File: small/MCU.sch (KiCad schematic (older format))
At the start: 35 parts, among them IC1 PIC32MX350F256H-V_PT, J3 Micro_SD_Card, J4 Conn_01x05_Female, U5 AT25M02, U8 PCF8563T, Y2 Crystal

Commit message: BOM updated
Layout changed
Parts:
- C15, C17, C18, C19, C20, C21, C24, C29, C30, C31: source (none) -> 0
- C25: source (none) -> 1
- C26, C44: value 15pf -> 20pf; MPN (none) -> CL10C200JB8NNNC; source (none) -> 0
- D10, D4: MPN (none) -> FC-2012HRK-620D; Price (none) -> 0.0199; source (none) -> 0
- D8: MPN (none) -> SS14; source (none) -> 0
- IC1: MPN (none) -> PIC32MX350F256H-V/PT; Manufacturer_Name Microchip -> (none); Manufacturer_Part_Number PIC32MX350F256H-V/PT -> (none)
- R24: MPN (none) -> 0603WAF1005T5E; Price (none) -> 0.0028; source (none) -> 0
- R39, R7: MPN (none) -> 0603WAF1000T5E; source (none) -> 0
- R5: MPN (none) -> 0603WAF1002T5E; source (none) -> 0
- R6: MPN (none) -> 0603WAF1001T5E; source (none) -> 0
- U5: Website (none) -> mouser; source (none) -> 0
- U8: MPN (none) -> PCF8563T; source (none) -> 0
- Y2: MPN (none) -> Q13FC1350000400; Price (none) -> 0.4291; source (none) -> 0
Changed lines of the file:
@@
 F 4 "C25804" H 1800 3350 50  0001 C CNN "LCSC"
 F 5 "0.02" H 1800 3350 50  0001 C CNN "Price"
+F 6 "0603WAF1002T5E" H 1800 3350 50  0001 C CNN "MPN"
+F 7 "0" H 1800 3350 50  0001 C CNN "source"
 	1    1800 3350
 	0    1    1    0
@@
 F 5 "0.0071" H 1075 3675 50  0001 C CNN "Price"
 F 6 "CC0603KRX7R9BB104" H 1075 3675 50  0001 C CNN "MPN"
+F 7 "0" H 1075 3675 50  0001 C CNN "source"
 	1    1075 3675
 	1    0    0    -1
@@
 F 4 " C21190" H 1800 3450 50  0001 C CNN "LCSC"
 F 5 "0.009" H 1800 3450 50  0001 C CNN "Price"
+F 6 "0603WAF1001T5E" H 1800 3450 50  0001 C CNN "MPN"
+F 7 "0" H 1800 3450 50  0001 C CNN "source"
 	1    1800 3450
 	0    1    1    0
@@
 F 3 "https://datasheet.lcsc.com/szlcsc/Foshan-NationStar-Optoelectronics-FC-2012HRK-620D_C84256.pdf" H 8125 3925 50  0001 C CNN
 F 4 "C84256" V 8125 3925 50  0001 C CNN "LCSC"
+F 5 "FC-2012HRK-620D" H 8125 3925 50  0001 C CNN "MPN"
+F 6 "0.0199" H 8125 3925 50  0001 C CNN "Price"
+F 7 "0" H 8125 3925 50  0001 C CNN "source"
 	1    8125 3925
 	0    -1   -1   0
@@
 F 4 "C22775" H 8125 4225 50  0001 C CNN "LCSC"
 F 5 "0.0019" H 8125 4225 50  0001 C CNN "Price"
+F 6 "0603WAF1000T5E" H 8125 4225 50  0001 C CNN "MPN"
+F 7 "0" H 8125 4225 50  0001 C CNN "source"
 	1    8125 4225
 	1    0    0    -1
@@
 F 4 "C7440" H 9975 5450 50  0001 C CNN "LCSC"
 F 5 "0.3876" H 9975 5450 50  0001 C CNN "Price"
+F 6 "PCF8563T" H 9975 5450 50  0001 C CNN "MPN"
+F 7 "0" H 9975 5450 50  0001 C CNN "source"
 	1    9975 5450
 	1    0    0    -1
@@
 AR Path="/6078415F/607D7927" Ref="C26"  Part="1"
 F 0 "C26" H 9315 5146 50  0000 L CNN
-F 1 "15pf" H 9315 5055 50  0000 L CNN
+F 1 "20pf" H 9315 5055 50  0000 L CNN
 F 2 "Capacitor_SMD:C_0603_1608Metric_Pad1.08x0.95mm_HandSolder" H 9238 4950 50  0001 C CNN
 F 3 "https://datasheet.lcsc.com/szlcsc/Samsung-Electro-Mechanics-CL10C150JB8NNNC_C1644.pdf" H 9200 5100 50  0001 C CNN
 F 4 "C1648" H 9200 5100 50  0001 C CNN "LCSC"
 F 5 "C1644" H 9200 5100 50  0001 C CNN "Price"
+F 6 "CL10C200JB8NNNC" H 9200 5100 50  0001 C CNN "MPN"
+F 7 "0" H 9200 5100 50  0001 C CNN "source"
 	1    9200 5100
 	1    0    0    -1
@@
 F 3 "https://datasheet.lcsc.com/szlcsc/1901081604_Seiko-Epson-Q13FC1350000400_C32346.pdf" H 9200 5450 50  0001 C CNN
 F 4 "C32346" V 9200 5450 50  0001 C CNN "LCSC"
+F 5 "Q13FC1350000400" H 9200 5450 50  0001 C CNN "MPN"
+F 6 "0.4291" H 9200 5450 50  0001 C CNN "Price"
+F 7 "0" H 9200 5450 50  0001 C CNN "source"
 	1    9200 5450
 	0    1    1    0
@@
 F 4 " C2480" H 9975 4550 50  0001 C CNN "LCSC"
 F 5 "0.0178" H 9975 4550 50  0001 C CNN "Price"
+F 6 "SS14" H 9975 4550 50  0001 C CNN "MPN"
+F 7 "0" H 9975 4550 50  0001 C CNN "source"
 	1    9975 4550
 	0    1    1    0
@@
 F 4 "KR-5R5C105-R" V 9050 4550 50  0001 C CNN "MPN"
 F 5 "C38065" H 9050 4550 50  0001 C CNN "LCSC"
+F 6 "1" H 9050 4550 50  0001 C CNN "source"
 	1    9050 4550
 	0    1    1    0
@@
 F 5 "AT25M02-SSHD-T" H 1650 7150 50  0001 C CNN "MPN"
 F 6 "2,60" H 1650 7150 50  0001 C CNN "Price"
+F 7 "mouser" H 1650 7150 50  0001 C CNN "Website"
+F 8 "0" H 1650 7150 50  0001 C CNN "source"
 	1    1650 7150
 	1    0    0    -1
@@
 F 3 "~" H 9725 4750 50  0001 C CNN
 F 4 " C7250" V 9725 4750 50  0001 C CNN "LCSC"
+F 5 "0603WAF1005T5E" H 9725 4750 50  0001 C CNN "MPN"
+F 6 "0.0028" H 9725 4750 50  0001 C CNN "Price"
+F 7 "0" H 9725 4750 50  0001 C CNN "source"
 	1    9725 4750
 	0    1    1    0
@@
 F 5 "0.0071" H 1075 2150 50  0001 C CNN "Price"
 F 6 "CC0603KRX7R9BB104" H 1075 2150 50  0001 C CNN "MPN"
+F 7 "0" H 1075 2150 50  0001 C CNN "source"
 	1    1075 2150
 	1    0    0    -1
@@
 F 5 "0.0071" H 1450 2150 50  0001 C CNN "Price"
 F 6 "CC0603KRX7R9BB104" H 1450 2150 50  0001 C CNN "MPN"
+F 7 "0" H 1450 2150 50  0001 C CNN "source"
 	1    1450 2150
 	1    0    0    -1
@@
 F 5 "0.0071" H 1825 2150 50  0001 C CNN "Price"
 F 6 "CC0603KRX7R9BB104" H 1825 2150 50  0001 C CNN "MPN"
+F 7 "0" H 1825 2150 50  0001 C CNN "source"
 	1    1825 2150
 	1    0    0    -1
@@
 F 5 "0.0071" H 2225 2150 50  0001 C CNN "Price"
 F 6 "CC0603KRX7R9BB104" H 2225 2150 50  0001 C CNN "MPN"
+F 7 "0" H 2225 2150 50  0001 C CNN "source"
 	1    2225 2150
 	1    0    0    -1
@@
 F 5 "0.0071" H 2600 2150 50  0001 C CNN "Price"
 F 6 "CC0603KRX7R9BB104" H 2600 2150 50  0001 C CNN "MPN"
+F 7 "0" H 2600 2150 50  0001 C CNN "source"
 	1    2600 2150
 	1    0    0    -1
@@
 F 5 "0.0071" H 8400 2800 50  0001 C CNN "Price"
 F 6 "CC0603KRX7R9BB104" H 8400 2800 50  0001 C CNN "MPN"
+F 7 "0" H 8400 2800 50  0001 C CNN "source"
 	1    8400 2800
 	1    0    0    -1
@@
 F 5 "TAJA106K016RNJ" H 5050 725 50  0001 C CNN "MPN"
 F 6 "0.2135" H 5050 725 50  0001 C CNN "Price"
+F 7 "0" H 5050 725 50  0001 C CNN "source"
 	1    5050 725
 	0    1    1    0
@@
 F 5 "0.0071" H 2125 3775 50  0001 C CNN "Price"
 F 6 "CC0603KRX7R9BB104" H 2125 3775 50  0001 C CNN "MPN"
+F 7 "0" H 2125 3775 50  0001 C CNN "source"
 	1    2125 3775
 	1    0    0    -1
@@
 F 5 "0.0071" H 2775 7150 50  0001 C CNN "Price"
 F 6 "CC0603KRX7R9BB104" H 2775 7150 50  0001 C CNN "MPN"
+F 7 "0" H 2775 7150 50  0001 C CNN "source"
 	1    2775 7150
 	1    0    0    -1
@@
 AR Path="/6078415F/609E1851" Ref="C44"  Part="1"
 F 0 "C44" H 9315 5846 50  0000 L CNN
-F 1 "15pf" H 9315 5755 50  0000 L CNN
+F 1 "20pf" H 9315 5755 50  0000 L CNN
 F 2 "Capacitor_SMD:C_0603_1608Metric_Pad1.08x0.95mm_HandSolder" H 9238 5650 50  0001 C CNN
 F 3 "https://datasheet.lcsc.com/szlcsc/Samsung-Electro-Mechanics-CL10C150JB8NNNC_C1644.pdf" H 9200 5800 50  0001 C CNN
 F 4 "C1648" H 9200 5800 50  0001 C CNN "LCSC"
 F 5 "C1644" H 9200 5800 50  0001 C CNN "Price"
+F 6 "CL10C200JB8NNNC" H 9200 5800 50  0001 C CNN "MPN"
+F 7 "0" H 9200 5800 50  0001 C CNN "source"
 	1    9200 5800
 	-1   0    0    1
@@
 F 3 "https://datasheet.lcsc.com/szlcsc/Foshan-NationStar-Optoelectronics-FC-2012HRK-620D_C84256.pdf" H 6200 875 50  0001 C CNN
 F 4 "C84256" V 6200 875 50  0001 C CNN "LCSC"
+F 5 "FC-2012HRK-620D" H 6200 875 50  0001 C CNN "MPN"
+F 6 "0.0199" H 6200 875 50  0001 C CNN "Price"
+F 7 "0" H 6200 875 50  0001 C CNN "source"
 	1    6200 875
 	-1   0    0    1
@@
 F 4 "C22775" H 6500 875 50  0001 C CNN "LCSC"
 F 5 "0.0019" H 6500 875 50  0001 C CNN "Price"
+F 6 "0603WAF1000T5E" H 6500 875 50  0001 C CNN "MPN"
+F 7 "0" H 6500 875 50  0001 C CNN "source"
 	1    6500 875
 	0    -1   -1   0
@@
 F 4 "Microchip PIC32MX350F256H-V/PT, 32bit PIC Microcontroller, 100MHz, 256 kB Flash, 64-Pin TQFP" H 6950 3850 50  0001 L CNN "Description"
 F 5 "1.2" H 6950 3750 50  0001 L CNN "Height"
-F 6 "Microchip" H 6950 3650 50  0001 L CNN "Manufacturer_Name"
-F 7 "PIC32MX350F256H-V/PT" H 6950 3550 50  0001 L CNN "Manufacturer_Part_Number"
+F 6 "" H 6950 3650 50  0001 L CNN "Manufacturer_Name"
+F 7 "" H 6950 3550 50  0001 L CNN "Manufacturer_Part_Number"
 F 8 "579-32MX350F256HVPT" H 6950 3450 50  0001 L CNN "Mouser Part Number"
 F 9 "https://www.mouser.com/Search/Refine.aspx?Keyword=579-32MX350F256HVPT" H 6950 3350 50  0001 L CNN "Mouser Price/Stock"
 F 10 "PIC32MX350F256H-V/PT" H 6950 3250 50  0001 L CNN "Arrow Part Number"
 F 11 "https://www.arrow.com/en/products/pic32mx350f256h-vpt/microchip-technology" H 6950 3150 50  0001 L CNN "Arrow Price/Stock"
+F 12 "PIC32MX350F256H-V/PT" H 3400 2850 50  0001 C CNN "MPN"
 	1    3400 2850
 	1    0    0    -1

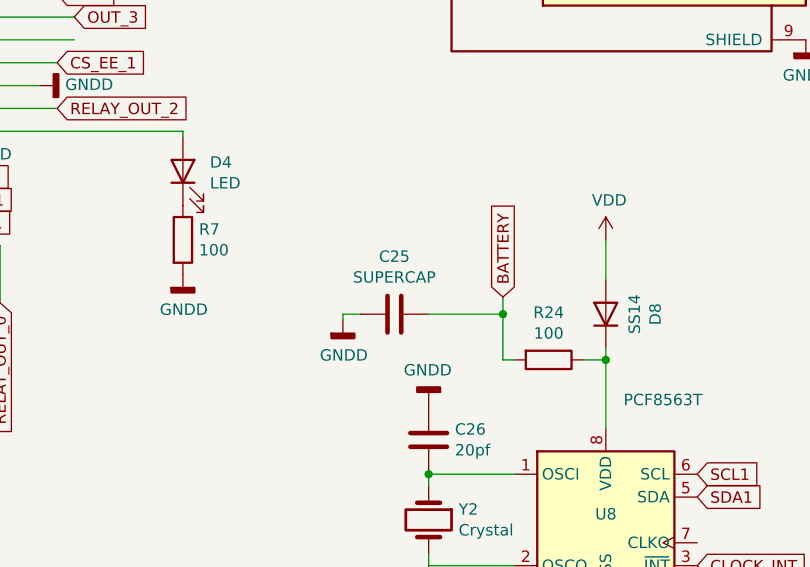
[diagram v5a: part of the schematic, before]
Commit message: Battery Footprint changed.
Few mods
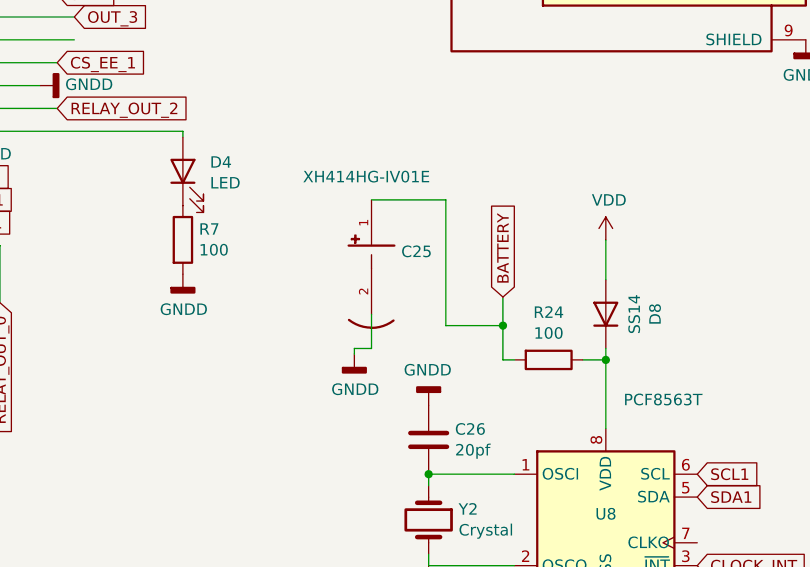
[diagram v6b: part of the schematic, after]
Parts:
- removed C25: SUPERCAP, small:XH414HG-IV01E, symbol Device:C
- added C25: XH414HG-IV01E, CAP_XH414HG-IV01E, symbol XH414HG-IV01E:XH414HG-IV01E
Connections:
- net BATTERY: now also C25.1
- net GND: now also C25.2
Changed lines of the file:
@@
 Wire Wire Line
 	9975 4225 9975 4400
-Wire Wire Line
-	9525 4750 9525 4550
 Text GLabel 9525 4475 1    50   Input ~ 0
 BATTERY
 $Comp
-L Device:C C?
-U 1 1 607D7962
-P 9050 4550
-AR Path="/607D7962" Ref="C?"  Part="1"
-AR Path="/6078415F/607D7962" Ref="C25"  Part="1"
-F 0 "C25" V 8798 4550 50  0000 C CNN
-F 1 "SUPERCAP" V 8889 4550 50  0000 C CNN
-F 2 "small:XH414HG-IV01E" H 9088 4400 50  0001 C CNN
-F 3 "~" H 9050 4550 50  0001 C CNN
-F 4 "KR-5R5C105-R" V 9050 4550 50  0001 C CNN "MPN"
-F 5 "C38065" H 9050 4550 50  0001 C CNN "LCSC"
-F 6 "1" H 9050 4550 50  0001 C CNN "source"
-	1    9050 4550
-	0    1    1    0
-$EndComp
-Wire Wire Line
-	9525 4550 9200 4550
-Connection ~ 9525 4550
-Wire Wire Line
-	9525 4550 9525 4475
-$Comp
 L power:GNDD #PWR?
 U 1 1 607D796B
-P 8825 4575
+P 8875 4725
 AR Path="/607D796B" Ref="#PWR?"  Part="1"
 AR Path="/6078415F/607D796B" Ref="#PWR075"  Part="1"
-F 0 "#PWR075" H 8825 4325 50  0001 C CNN
-F 1 "GNDD" H 8829 4420 50  0000 C CNN
-F 2 "" H 8825 4575 50  0001 C CNN
-F 3 "" H 8825 4575 50  0001 C CNN
-	1    8825 4575
-	1    0    0    -1
-$EndComp
-Wire Wire Line
-	8900 4550 8825 4550
-Wire Wire Line
-	8825 4550 8825 4575
+F 0 "#PWR075" H 8875 4475 50  0001 C CNN
+F 1 "GNDD" H 8879 4570 50  0000 C CNN
+F 2 "" H 8875 4725 50  0001 C CNN
+F 3 "" H 8875 4725 50  0001 C CNN
+	1    8875 4725
+	1    0    0    -1
+$EndComp
+Wire Wire Line
+	8950 4700 8875 4700
+Wire Wire Line
+	8875 4700 8875 4725
 $Comp
 L Memory_EEPROM:AT25xxx U?
@@
 Wire Wire Line
 	3400 4350 3400 4975
+Wire Wire Line
+	9525 4475 9525 4600
+$Comp
+L XH414HG-IV01E:XH414HG-IV01E C25
+U 1 1 604D57EE
+P 8950 4250
+F 0 "C25" H 9080 4223 50  0000 L CNN
+F 1 "XH414HG-IV01E" H 8650 4550 50  0000 L CNN
+F 2 "CAP_XH414HG-IV01E" H 8950 4250 50  0001 L BNN
+F 3 "" H 8950 4250 50  0001 L BNN
+F 4 "Seiko" H 8950 4250 50  0001 L BNN "MANUFACTURER"
+F 5 "C38065" H 8950 4250 50  0001 C CNN "LCSC"
+F 6 "XH414HG-IV01E" H 8950 4250 50  0001 C CNN "MPN"
+	1    8950 4250
+	1    0    0    -1
+$EndComp
+Wire Wire Line
+	8950 4700 8950 4550
+Wire Wire Line
+	8950 4050 9275 4050
+Wire Wire Line
+	9275 4050 9275 4600
+Wire Wire Line
+	9275 4600 9525 4600
+Connection ~ 9525 4600
+Wire Wire Line
+	9525 4600 9525 4750
 $EndSCHEMATC
